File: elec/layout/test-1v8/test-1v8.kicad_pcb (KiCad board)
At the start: 2 copper layers, 8 parts, among them U3 10µH ±20%

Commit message: building successfully
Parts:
- R1: value 10kΩ ±1% 62.5mW -> 8.06kΩ ±1% 62.5mW
- R2: value 13kΩ ±1% 62.5mW -> 10kΩ ±1% 62.5mW
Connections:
- C2 pad 1: hv -> hv-1
- C2 pad 2: gnd -> gnd-1
- C3 pad 1: hv-1 -> hv
- C3 pad 2: gnd-1 -> gnd
- R1 pad 2: gnd-1 -> gnd
- R2 pad 1: hv-1 -> hv
- U1 pad 2: gnd-1 -> gnd
- U2 pad 2: gnd -> gnd-1
- U2 pad 4: hv -> hv-1
- U2 pad 5: hv -> hv-1
- U3 pad 2: hv-1 -> hv
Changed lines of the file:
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@@
             (outputdirectory "")))
     (net 0 "")
-    (net 1 "gnd")
+    (net 1 "gnd-1")
     (net 2 "line")
     (net 3 "SW")
-    (net 4 "hv")
+    (net 4 "hv-1")
     (net 5 "CB")
-    (net 6 "gnd-1")
-    (net 7 "hv-1")
+    (net 6 "gnd")
+    (net 7 "hv")
     (footprint "atopile:C0805-3b2e55"
         (layer "F.Cu")
@@
             (layers "F.Cu" "F.Paste" "F.Mask")
             (remove_unused_layers no)
-            (net 6 "gnd-1"))
+            (net 6 "gnd"))
         (pad "1" smd rect
             (at -1 0 0)
@@
             (layers "F.Cu" "F.Paste" "F.Mask")
             (remove_unused_layers no)
-            (net 7 "hv-1")))
+            (net 7 "hv")))
     (footprint "atopile:R0402-56259e"
         (layer "F.Cu")
@@
                     (thickness 0.15))
                 (hide no)))
-        (property "Value" "13kΩ ±1% 62.5mW"
+        (property "Value" "10kΩ ±1% 62.5mW"
             (at 0 4 0)
             (layer "F.Fab")
@@
                     (size 0.125 0.125)
                     (thickness 0.01875))))
-        (property "LCSC" "C138057"
-            (at 0 0 0)
-            (layer "User.9")
-            (hide yes)
-            (effects
-                (font
-                    (size 0.125 0.125)
-                    (thickness 0.01875))))
-        (property "Partnumber" "RC0402FR-0713KL"
-            (at 0 0 0)
-            (layer "User.9")
-            (hide yes)
-            (effects
-                (font
-                    (size 0.125 0.125)
-                    (thickness 0.01875))))
-        (property "Manufacturer" "YAGEO"
-            (at 0 0 0)
-            (layer "User.9")
-            (hide yes)
-            (effects
-                (font
-                    (size 0.125 0.125)
-                    (thickness 0.01875))))
-        (property "JLCPCB description" "62.5mW Thick Film Resistors 50V ±100ppm/℃ ±1% 13kΩ 0402 Chip Resistor - Surface Mount ROHS"
+        (property "LCSC" "C25744"
+            (at 0 0 0)
+            (layer "User.9")
+            (hide yes)
+            (effects
+                (font
+                    (size 0.125 0.125)
+                    (thickness 0.01875))))
+        (property "Partnumber" "0402WGF1002TCE"
+            (at 0 0 0)
+            (layer "User.9")
+            (hide yes)
+            (effects
+                (font
+                    (size 0.125 0.125)
+                    (thickness 0.01875))))
+        (property "Manufacturer" "UNI-ROYAL(Uniroyal Elec)"
+            (at 0 0 0)
+            (layer "User.9")
+            (hide yes)
+            (effects
+                (font
+                    (size 0.125 0.125)
+                    (thickness 0.01875))))
+        (property "JLCPCB description" "62.5mW Thick Film Resistors 50V ±100ppm/℃ ±1% 10kΩ 0402 Chip Resistor - Surface Mount ROHS"
             (at 0 0 0)
             (layer "User.9")
@@
             (layers "F.Cu" "F.Paste" "F.Mask")
             (remove_unused_layers no)
-            (net 7 "hv-1")))
+            (net 7 "hv")))
     (footprint "atopile:C0402-b3ef17"
         (layer "F.Cu")
@@
             (layers "F.Cu" "F.Paste" "F.Mask")
             (remove_unused_layers no)
-            (net 1 "gnd"))
+            (net 1 "gnd-1"))
         (pad "1" smd rect
             (at 1.35 0.95 0)
@@
             (layers "F.Cu" "F.Paste" "F.Mask")
             (remove_unused_layers no)
-            (net 4 "hv"))
+            (net 4 "hv-1"))
         (pad "4" smd rect
             (at -1.35 -0.95 0)
@@
             (layers "F.Cu" "F.Paste" "F.Mask")
             (remove_unused_layers no)
-            (net 4 "hv"))
+            (net 4 "hv-1"))
         (model "${KIPRJMOD}/../../../build/footprints/footprints.3dshapes/SOT-23-6_L2.9-W1.6-H1.5-LS2.8-P0.95.step"
             (offset
@@
             (layers "F.Cu" "F.Paste" "F.Mask")
             (remove_unused_layers no)
-            (net 7 "hv-1"))
+            (net 7 "hv"))
         (pad "1" smd rect
             (at -1.6 0 0)
@@
             (layers "F.Cu" "F.Paste" "F.Mask")
             (remove_unused_layers no)
-            (net 6 "gnd-1"))
+            (net 6 "gnd"))
         (pad "1" smd rect
             (at -1.17 0 0)
@@
             (layers "F.Cu" "F.Paste" "F.Mask")
             (remove_unused_layers no)
-            (net 1 "gnd"))
+            (net 1 "gnd-1"))
         (pad "1" smd rect
             (at -1 0 0)
@@
             (layers "F.Cu" "F.Paste" "F.Mask")
             (remove_unused_layers no)
-            (net 4 "hv")))
+            (net 4 "hv-1")))
     (footprint "atopile:R0402-56259e"
         (layer "F.Cu")
@@
                     (thickness 0.15))
                 (hide no)))
-        (property "Value" "10kΩ ±1% 62.5mW"
+        (property "Value" "8.06kΩ ±1% 62.5mW"
             (at 0 4 0)
             (layer "F.Fab")
@@
                     (size 0.125 0.125)
                     (thickness 0.01875))))
-        (property "LCSC" "C25744"
-            (at 0 0 0)
-            (layer "User.9")
-            (hide yes)
-            (effects
-                (font
-                    (size 0.125 0.125)
-                    (thickness 0.01875))))
-        (property "Partnumber" "0402WGF1002TCE"
-            (at 0 0 0)
-            (layer "User.9")
-            (hide yes)
-            (effects
-                (font
-                    (size 0.125 0.125)
-                    (thickness 0.01875))))
-        (property "Manufacturer" "UNI-ROYAL(Uniroyal Elec)"
-            (at 0 0 0)
-            (layer "User.9")
-            (hide yes)
-            (effects
-                (font
-                    (size 0.125 0.125)
-                    (thickness 0.01875))))
-        (property "JLCPCB description" "62.5mW Thick Film Resistors 50V ±100ppm/℃ ±1% 10kΩ 0402 Chip Resistor - Surface Mount ROHS"
+        (property "LCSC" "C4250245"
+            (at 0 0 0)
+            (layer "User.9")
+            (hide yes)
+            (effects
+                (font
+                    (size 0.125 0.125)
+                    (thickness 0.01875))))
+        (property "Partnumber" "CRCW04028K06FKEDC"
+            (at 0 0 0)
+            (layer "User.9")
+            (hide yes)
+            (effects
+                (font
+                    (size 0.125 0.125)
+                    (thickness 0.01875))))
+        (property "Manufacturer" "Vishay Intertech"
+            (at 0 0 0)
+            (layer "User.9")
+            (hide yes)
+            (effects
+                (font
+                    (size 0.125 0.125)
+                    (thickness 0.01875))))
+        (property "JLCPCB description" "62.5mW Thick Film Resistors ±100ppm/℃ ±1% 8.06kΩ 0402  Chip Resistor - Surface Mount ROHS"
             (at 0 0 0)
             (layer "User.9")
@@
             (layers "F.Cu" "F.Paste" "F.Mask")
             (remove_unused_layers no)
-            (net 6 "gnd-1"))
+            (net 6 "gnd"))
         (pad "1" smd rect
             (at -0.43 0 0)

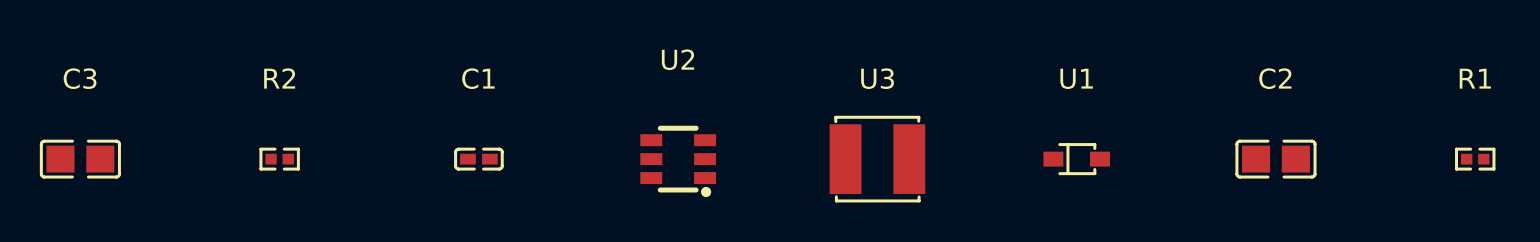
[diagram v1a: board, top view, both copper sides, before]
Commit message: Update layouts to kicad 9, add default build for layout reuse
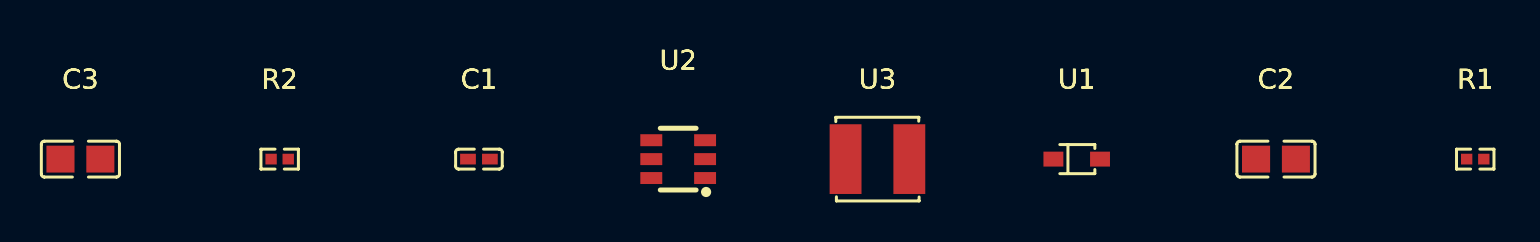
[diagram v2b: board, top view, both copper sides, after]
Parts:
- C2: value 10µF ±10% 25V X5R -> 4.7µF ±10% 25V X5R
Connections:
- net line renamed FB
